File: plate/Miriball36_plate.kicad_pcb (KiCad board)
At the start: 2 copper layers, 124.7 x 99.1 mm, 4 parts

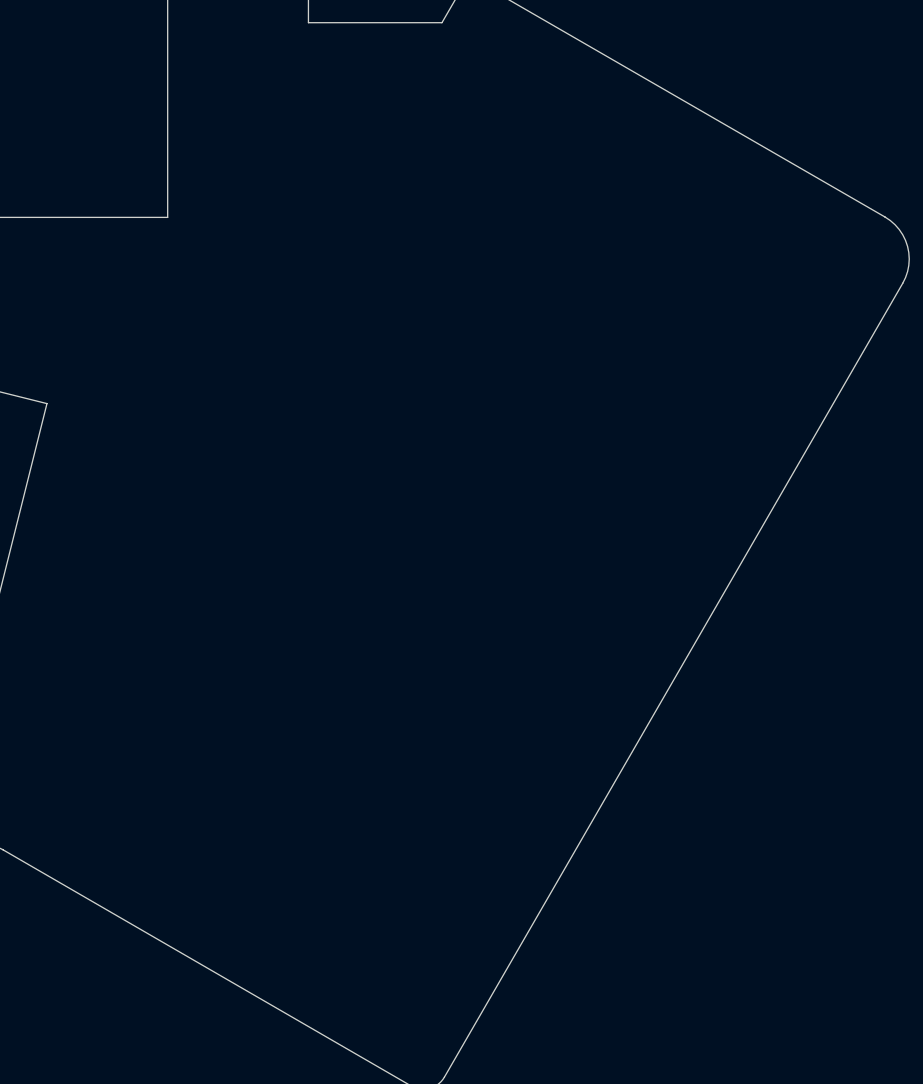
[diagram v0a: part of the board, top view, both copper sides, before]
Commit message: add hole
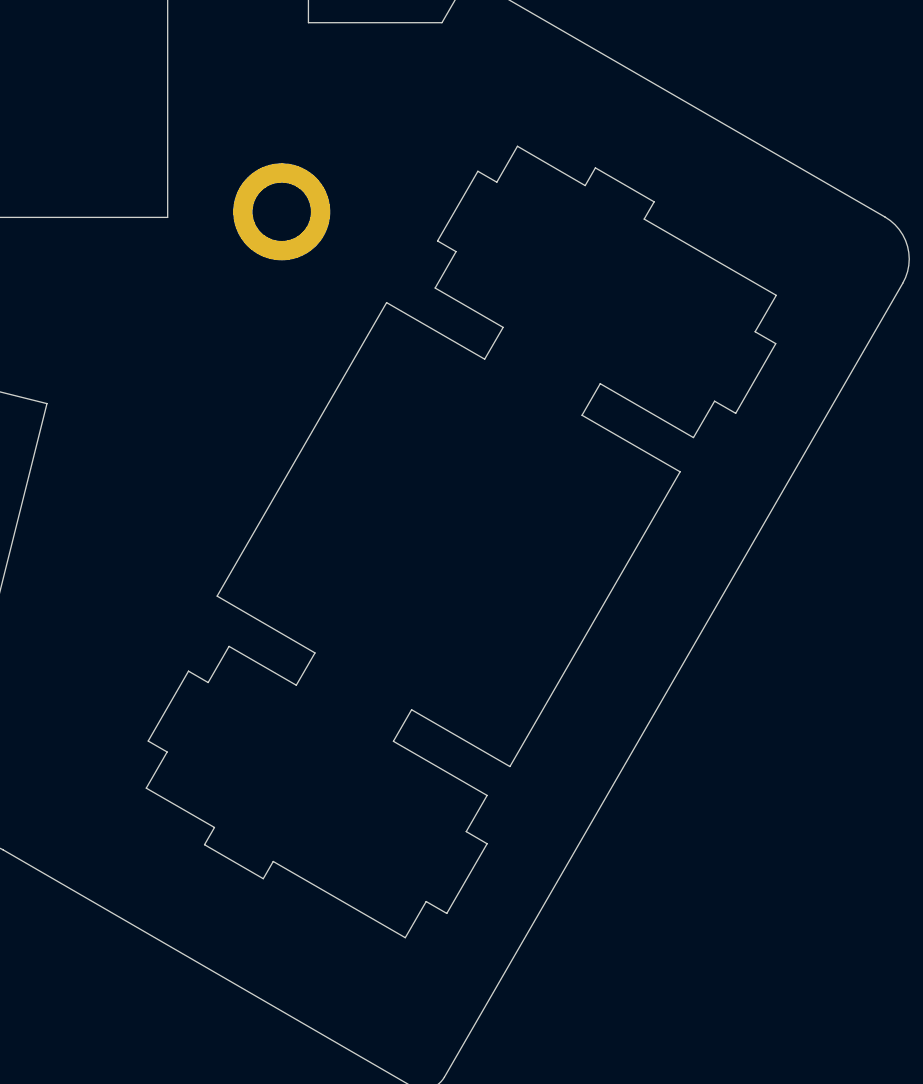
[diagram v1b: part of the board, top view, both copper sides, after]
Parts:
- added H4: MountingHole, Miriball36:HOLE_M2_CASEPCB, F.Cu at (145.7, 101.0)
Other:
- outline, holes or cut-outs redrawn
